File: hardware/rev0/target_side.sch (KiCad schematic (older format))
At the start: 31 parts, among them IC1 ECP5-BGA256, U1 2450FB15A050, U12 0896BM15E0025, U13 TXETALSANF-26.000000, U9 AT86RF215

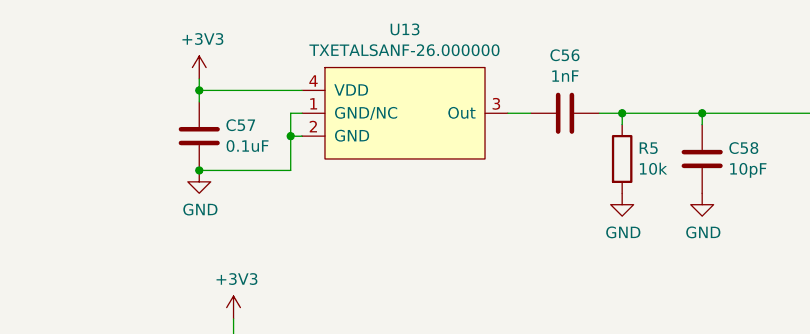
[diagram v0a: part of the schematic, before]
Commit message: Swap TCXO for one available on Mouser
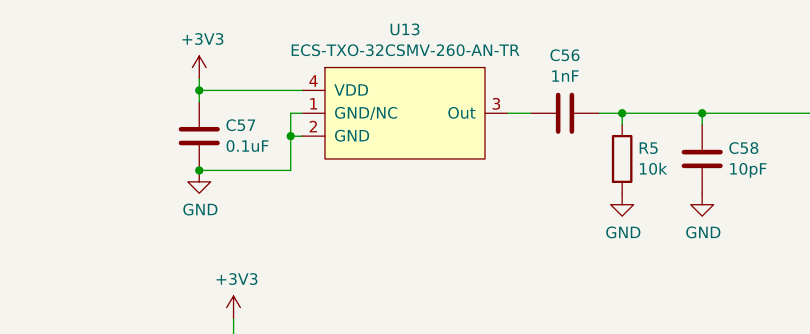
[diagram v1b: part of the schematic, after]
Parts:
- U13: value TXETALSANF-26.000000 -> ECS-TXO-32CSMV-260-AN-TR
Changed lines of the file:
@@
 P 2400 1350
 F 0 "U13" H 2400 1715 50  0000 C CNN
-F 1 "TXETALSANF-26.000000" H 2400 1624 50  0000 C CNN
+F 1 "ECS-TXO-32CSMV-260-AN-TR " H 2400 1624 50  0000 C CNN
 F 2 "Oscillator:Oscillator_SMD_SeikoEpson_SG8002CE-4Pin_3.2x2.5mm" H 2450 1850 50  0001 C CNN
 F 3 "" H 2450 1850 50  0001 C CNN

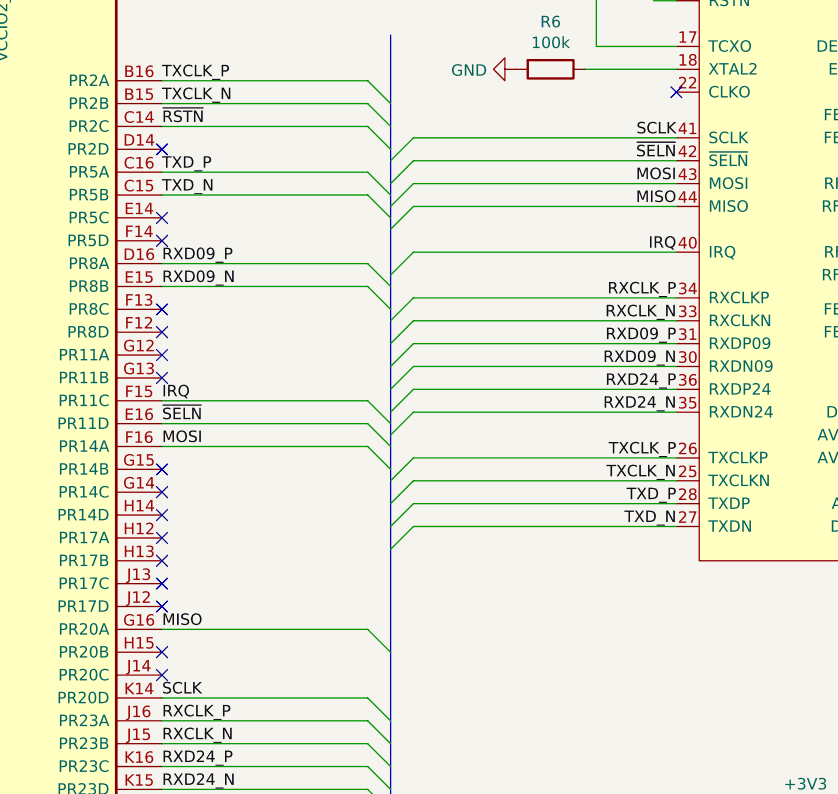
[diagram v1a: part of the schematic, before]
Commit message: hardware: adopt OSHWA convention for SPI signal names
https://www.oshwa.org/a-resolution-to-redefine-spi-signal-names
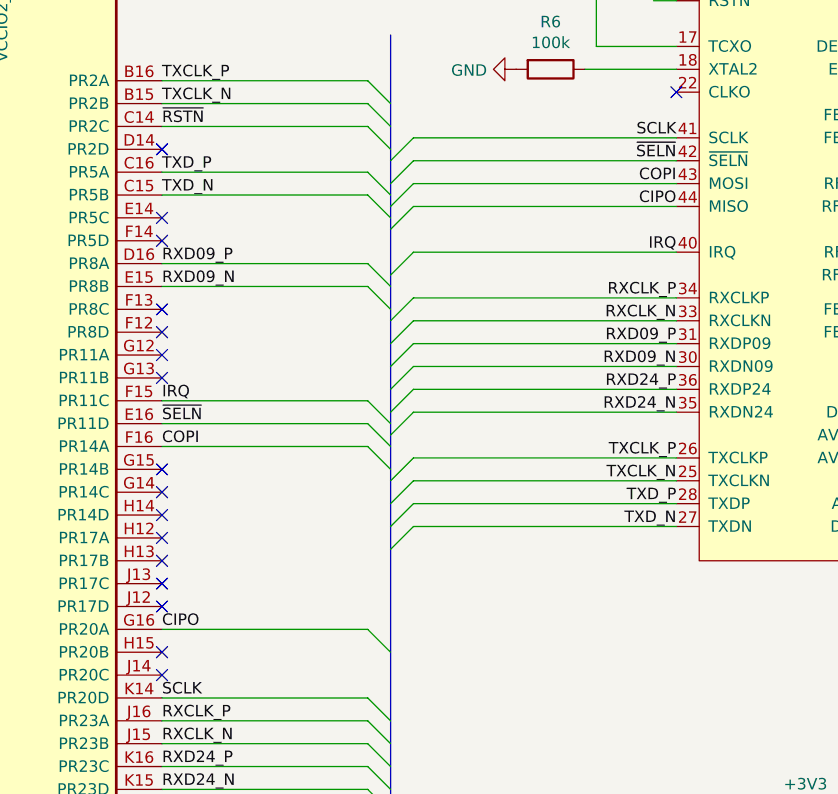
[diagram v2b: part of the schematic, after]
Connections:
- net MISO renamed CIPO
- net MOSI renamed COPI
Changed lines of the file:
@@
 ~SELN
 Text Label 4650 3550 2    50   ~ 0
-MOSI
+COPI
 Text Label 4650 3650 2    50   ~ 0
-MISO
+CIPO
 Text Notes 8550 2500 0    50   ~ 0
 TODO: swap 24/09 position to match physical layout
@@
 ~SELN
 Text Label 2400 4700 0    50   ~ 0
-MOSI
+COPI
 Text Label 2400 5500 0    50   ~ 0
-MISO
+CIPO
 Text HLabel 10400 2950 2    50   Input ~ 0
 RF24
